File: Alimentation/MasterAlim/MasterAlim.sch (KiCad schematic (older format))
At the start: 42 parts, among them J1 Ext-Con, J10 Interf-Reg1, J11 AU Logic, J12 Interf-Reg2, J13 Interf-Reg3, J14 Interf-Reg4, J3 Bat. IN, J5 Direct Out, J6 Reg 1, J7 Reg 2, J8 Reg 3, J9 Reg 4, U1 74LS33, U3 ACS712xLCTR-20A, U6 PTN78020W_EUK-7, U7 ACS712xLCTR-20A

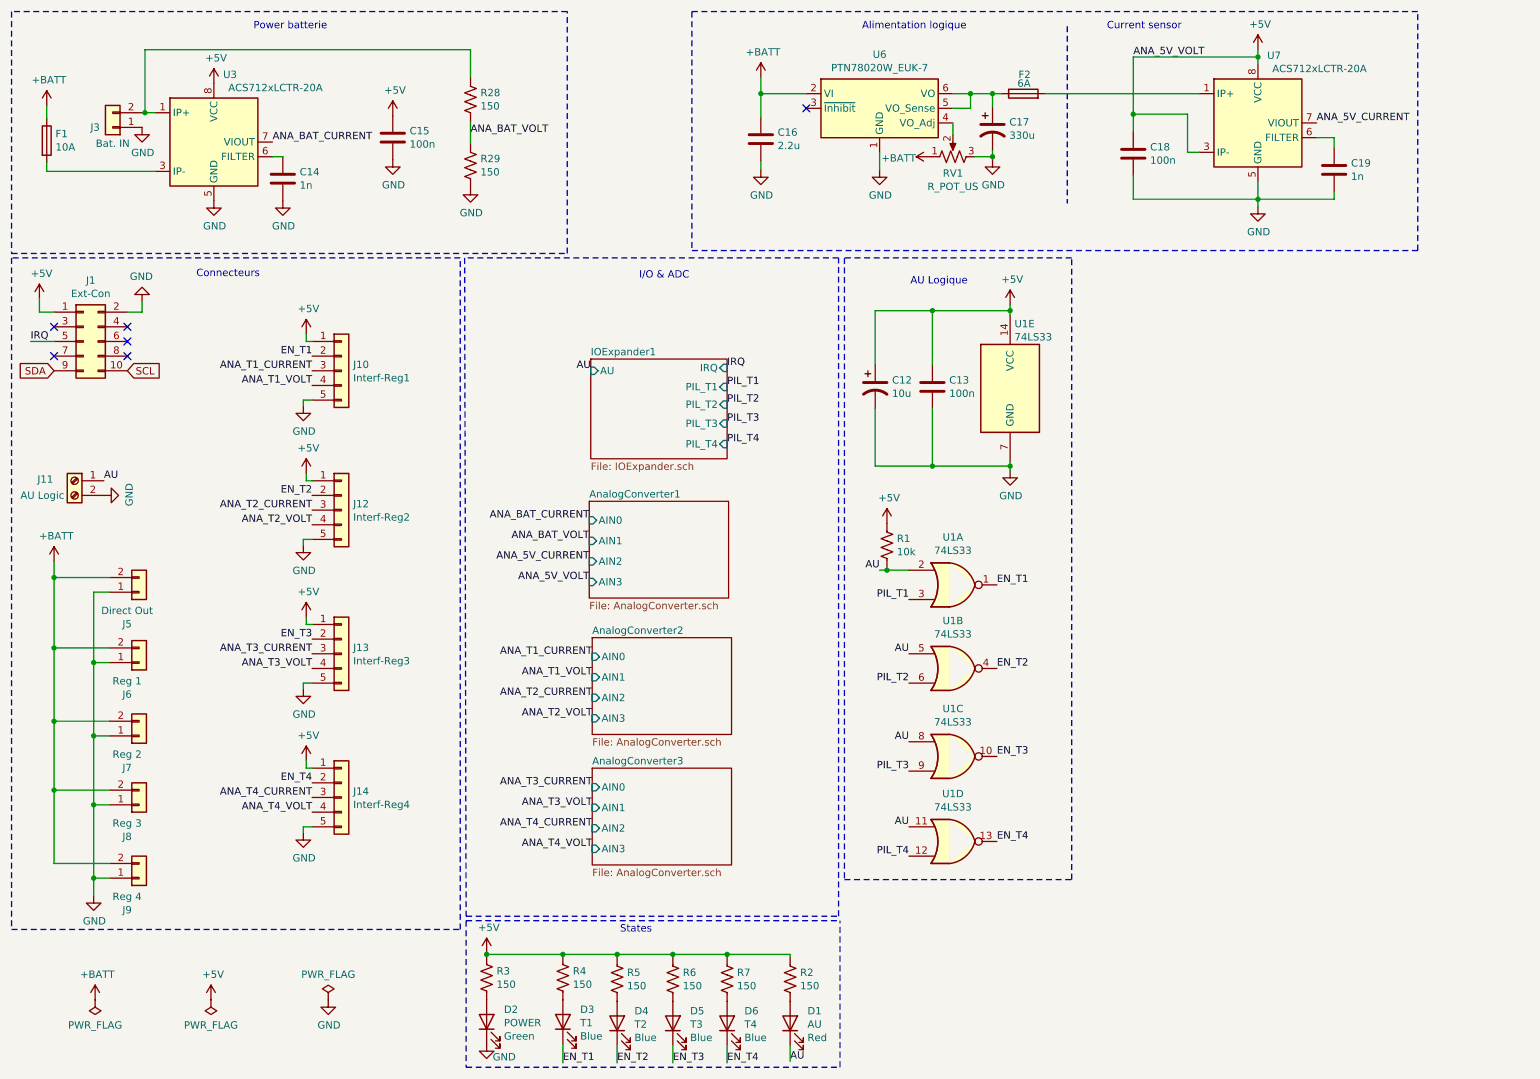
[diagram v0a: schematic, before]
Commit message: Dimensionnement et récupération des part LCSC
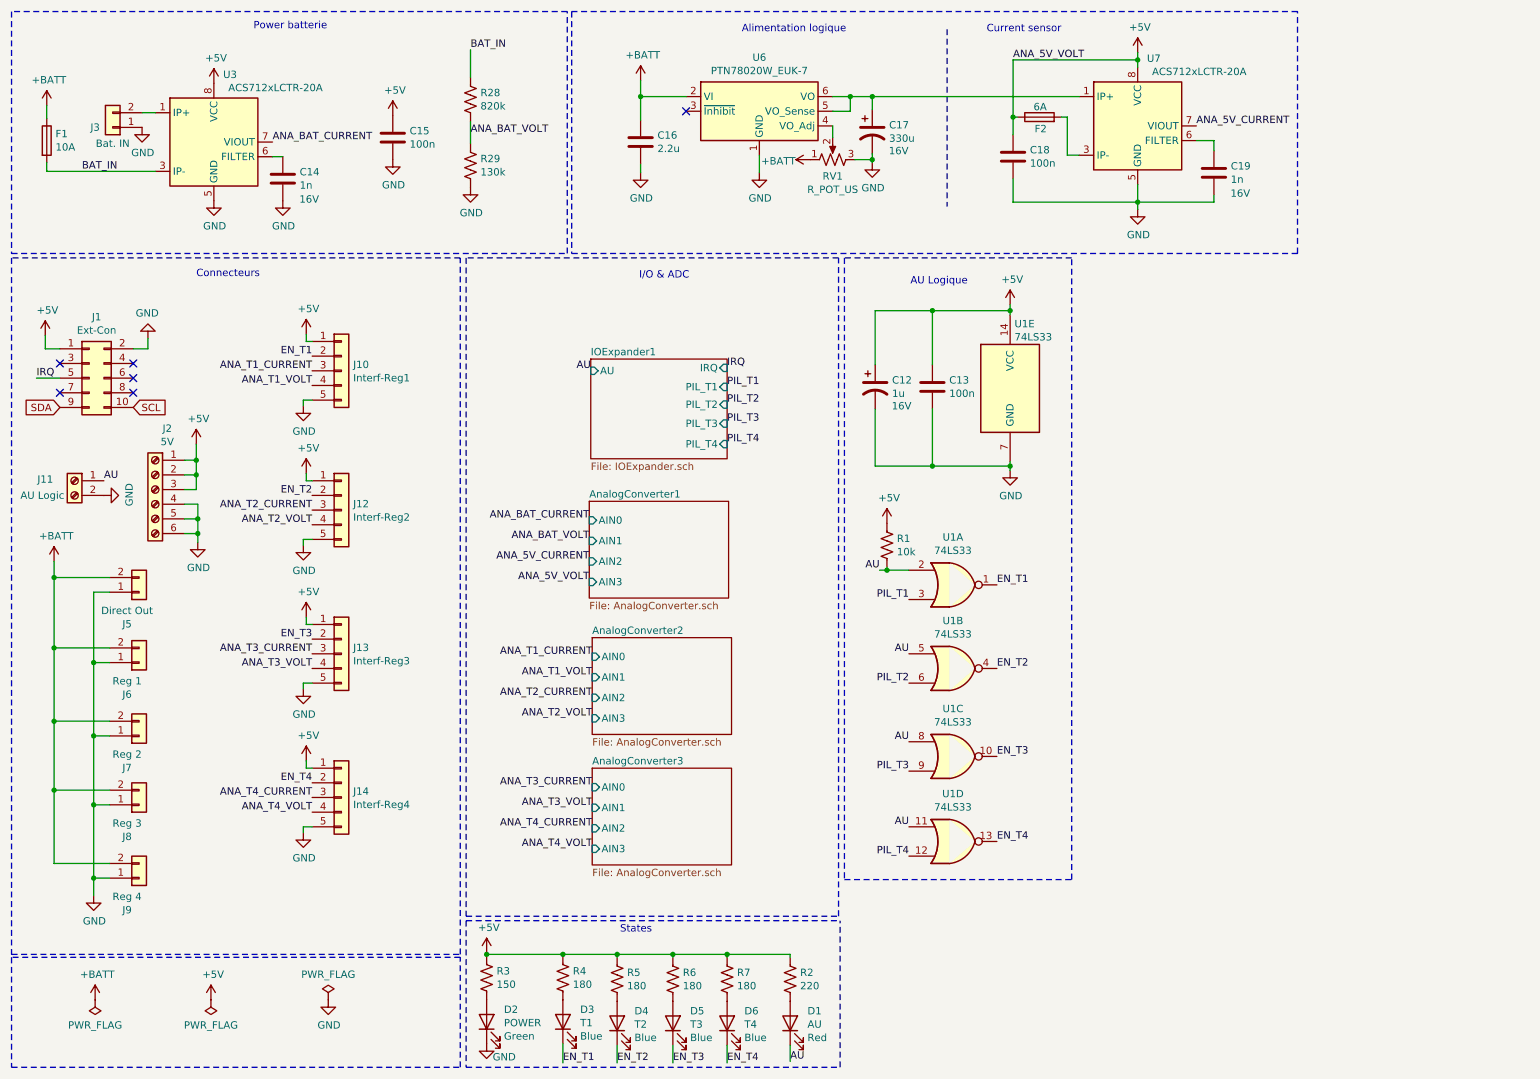
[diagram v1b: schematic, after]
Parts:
- added J2: 5V, TerminalBlock_Phoenix:TerminalBlock_Phoenix_MPT-0,5-6-2.54_1x06_P2.54mm_Horizontal, symbol Connector:Screw_Terminal_01x06
- C12: value 10u -> 1u; footprint (none) -> Capacitor_SMD:CP_Elec_4x5.3; LCSC Part (none) -> C249445; Tension (none) -> 16V
- C13, C15, C18: footprint Capacitor_SMD:C_0805_2012Metric -> Capacitor_SMD:C_0805_2012Metric_Pad1.18x1.45mm_HandSolder; LCSC Part (none) -> C28233
- C14: footprint (none) -> Capacitor_SMD:C_0603_1608Metric_Pad1.08x0.95mm_HandSolder; LCSC (none) -> C163169; Tension (none) -> 16V
- C16: footprint (none) -> Capacitor_SMD:C_0805_2012Metric_Pad1.18x1.45mm_HandSolder; LCSC Part (none) -> C508857; Tension (none) -> 50V
- C17: footprint (none) -> Capacitor_SMD:CP_Elec_10x10; LCSC Part (none) -> C249905; Tension (none) -> 16V
- C19: footprint (none) -> Capacitor_SMD:C_0603_1608Metric_Pad1.08x0.95mm_HandSolder; LCSC Part (none) -> C163169; Tension (none) -> 16V
- D1: LCSC Part (none) -> C72037
- D2: LCSC Part (none) -> C205442
- D3, D4, D5, D6: LCSC Part (none) -> C205441
- F1, F2, J1, J11, J3, J5, J6, J7, J8, J9, U1: JLCPCB BOM (none) -> 0
- J10, J12, J13, J14: footprint Connector_JST:JST_EH_S5B-EH_1x05_P2.50mm_Horizontal -> Connector_JST:JST_PH_B5B-PH-K_1x05_P2.00mm_Vertical; JLCPCB BOM (none) -> 0
- R1: footprint Resistor_SMD:R_0805_2012Metric -> Resistor_SMD:R_0805_2012Metric_Pad1.20x1.40mm_HandSolder; LCSC Part (none) -> C17414
- R2: value 150 -> 220; footprint Resistor_SMD:R_0805_2012Metric -> Resistor_SMD:R_0805_2012Metric_Pad1.20x1.40mm_HandSolder; LCSC Part (none) -> C417010
- R28: value 150 -> 820k; footprint Resistor_SMD:R_0805_2012Metric -> Resistor_SMD:R_0805_2012Metric_Pad1.20x1.40mm_HandSolder; LCSC Part (none) -> C334983
- R29: value 150 -> 130k; footprint Resistor_SMD:R_0805_2012Metric -> Resistor_SMD:R_0805_2012Metric_Pad1.20x1.40mm_HandSolder; LCSC Part (none) -> C25617
- R3: footprint Resistor_SMD:R_0805_2012Metric -> Resistor_SMD:R_0805_2012Metric_Pad1.20x1.40mm_HandSolder; LCSC Part (none) -> C17471
- R4, R5, R6, R7: value 150 -> 180; footprint Resistor_SMD:R_0805_2012Metric -> Resistor_SMD:R_0805_2012Metric_Pad1.20x1.40mm_HandSolder; LCSC Part (none) -> C168485
- RV1: footprint Potentiometer_THT:Potentiometer_Bourns_3299Y_Vertical -> Potentiometer_SMD:Potentiometer_Bourns_TC33X_Vertical; LCSC Part (none) -> C719177
- U6: footprint Module:Texas_EUK_R-PDSS-T7_THT -> ARIG:Texas_EUK_R-PDSS-T7_THT; JLCPCB BOM (none) -> 0
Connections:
- net +5V: now also F2.1, J2.1 (Pin_1), J2.2 (Pin_2), J2.3 (Pin_3); no longer U7.3 (IP-), U7.4 (IP-)
- net GND: now also J2.4 (Pin_4), J2.5 (Pin_5), J2.6 (Pin_6)
- net at J3.2 (Pin_2), U3.1 (IP+), U3.2 (IP+): no longer R28.1
- net at C17.1, U6.5 (VO_Sense), U6.6 (VO): now also U7.1 (IP+), U7.2 (IP+); no longer F2.1
- net BAT_IN: now reaches F1.2, U3.3 (IP-), U3.4 (IP-)
- net BAT_IN: now also R28.1
- new net: F2.2, U7.3 (IP-), U7.4 (IP-)
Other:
- moved on the sheet: C16, C17, C18, C19, F2, J1, RV1, U6, U7

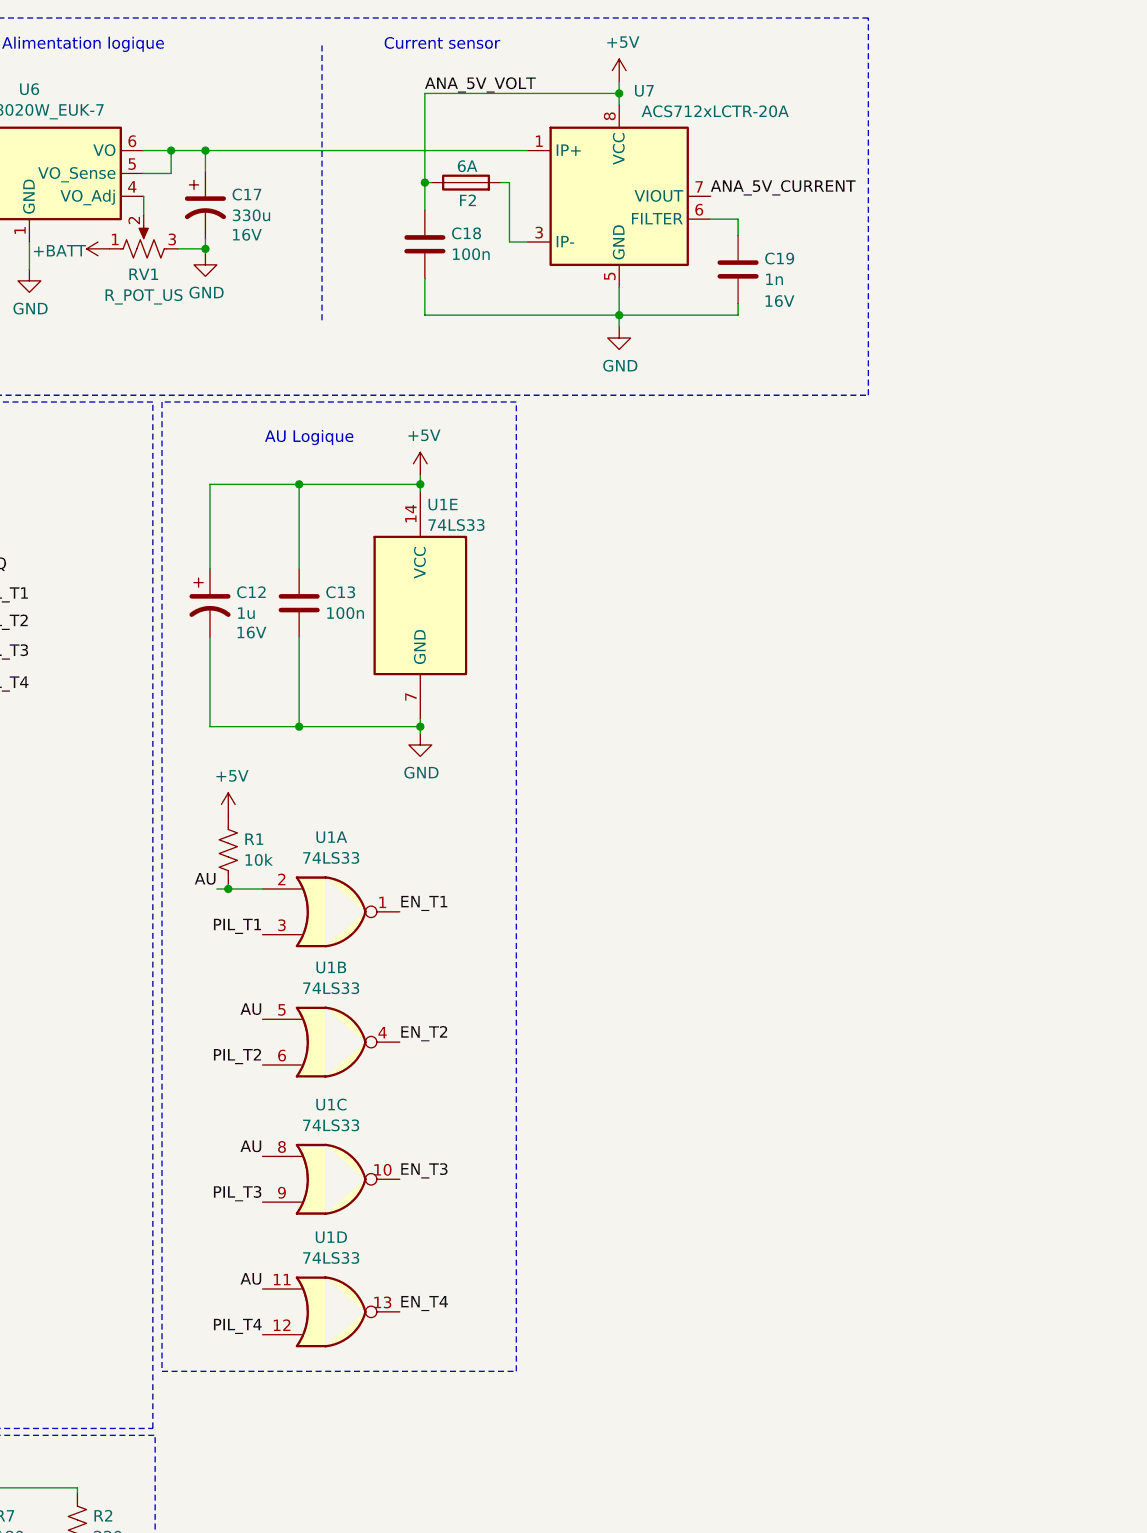
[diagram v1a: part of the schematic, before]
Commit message: Finalisation routage carte alim maitre
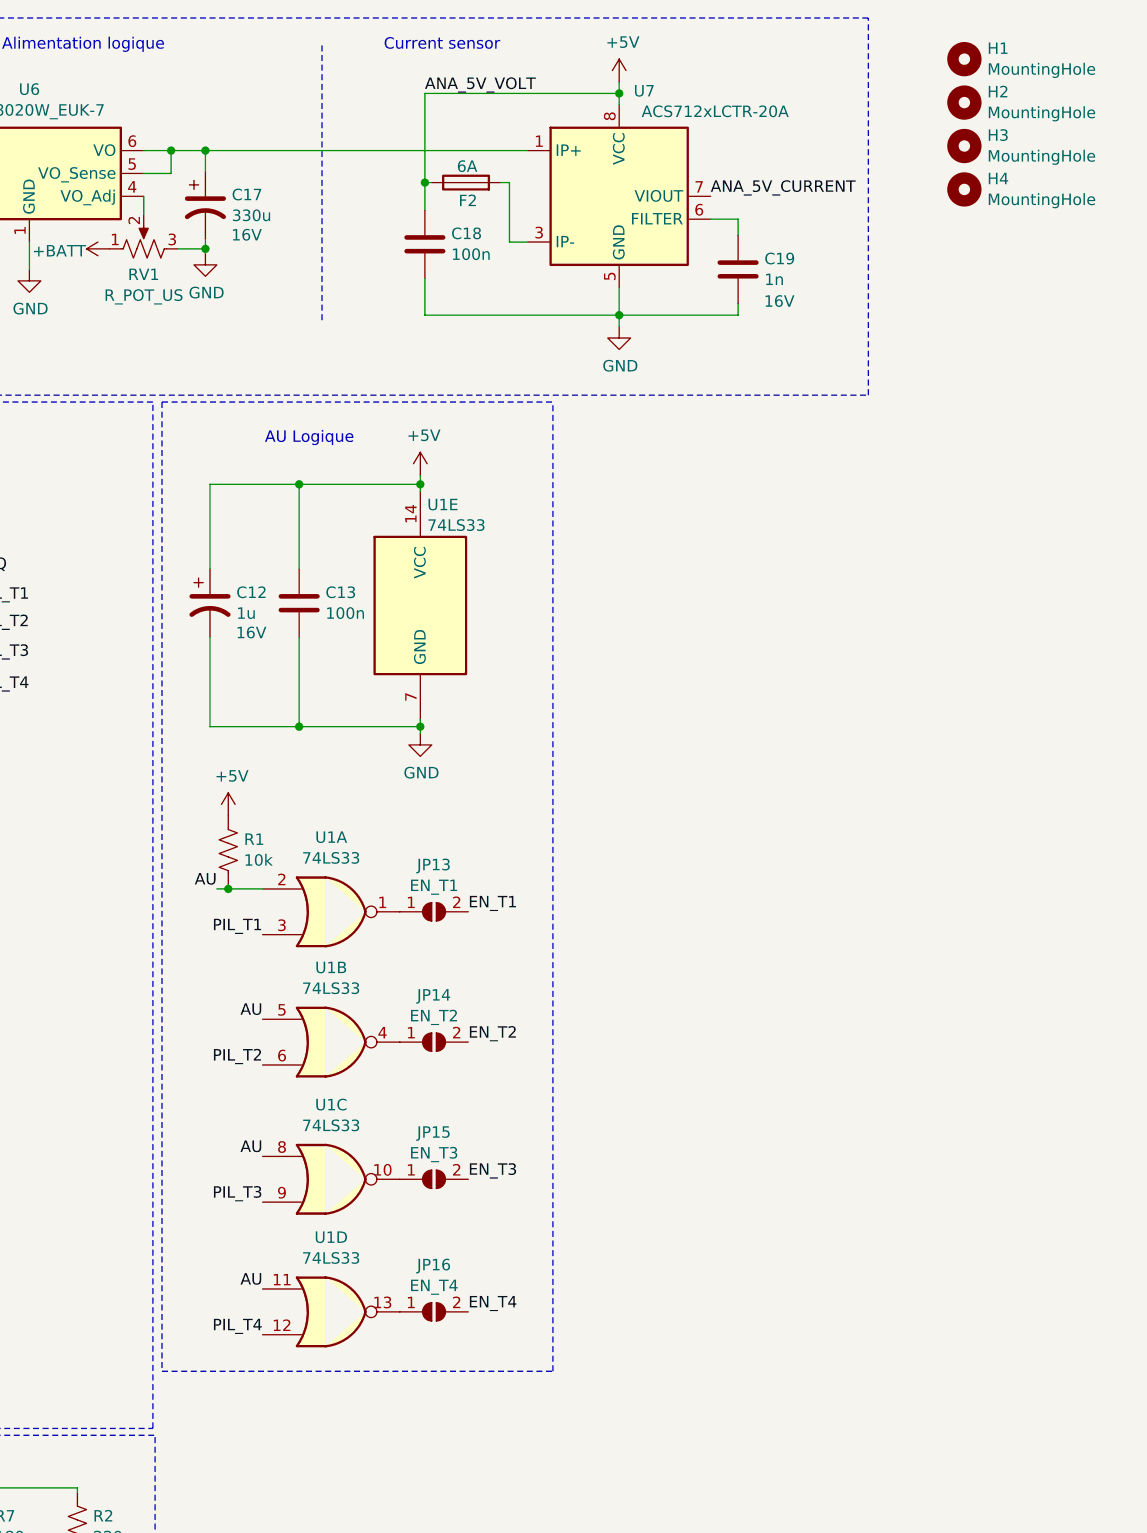
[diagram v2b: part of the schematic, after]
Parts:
- added H1, H2, H3, H4: MountingHole, MountingHole:MountingHole_3.2mm_M3, symbol Mechanical:MountingHole
- added JP13: EN_T1, Jumper:SolderJumper-2_P1.3mm_Open_RoundedPad1.0x1.5mm, symbol Jumper:SolderJumper_2_Open
- added JP14: EN_T2, Jumper:SolderJumper-2_P1.3mm_Open_RoundedPad1.0x1.5mm, symbol Jumper:SolderJumper_2_Open
- added JP15: EN_T3, Jumper:SolderJumper-2_P1.3mm_Open_RoundedPad1.0x1.5mm, symbol Jumper:SolderJumper_2_Open
- added JP16: EN_T4, Jumper:SolderJumper-2_P1.3mm_Open_RoundedPad1.0x1.5mm, symbol Jumper:SolderJumper_2_Open
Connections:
- net EN_T1: now also JP13.2 (B); no longer U1.1
- net EN_T2: now also JP14.2 (B); no longer U1.4
- net EN_T3: now also JP15.2 (B); no longer U1.10
- net EN_T4: now also JP16.2 (B); no longer U1.13
- new net: JP13.1 (A), U1.1
- new net: JP14.1 (A), U1.4
- new net: JP15.1 (A), U1.10
- new net: JP16.1 (A), U1.13
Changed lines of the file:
@@
 Text Label 7010 6320 2    50   ~ 0
 PIL_T4
-Text Label 7610 6220 0    50   ~ 0
+Text Label 7910 6220 0    50   ~ 0
 EN_T4
-Text Label 7610 5640 0    50   ~ 0
+Text Label 7910 5640 0    50   ~ 0
 EN_T3
-Text Label 7610 4470 0    50   ~ 0
+Text Label 7910 4470 0    50   ~ 0
 EN_T1
 Wire Notes Line
-	6570 6480 8120 6480
-Wire Notes Line
-	8120 6480 8120 2240
-Wire Notes Line
-	8120 2240 6570 2240
+	6570 6480 8280 6480
+Wire Notes Line
+	8280 6480 8280 2250
 Wire Notes Line
 	6570 2240 6570 6480
@@
 Wire Wire Line
 	5770 7010 5770 6990
-Text Label 7610 5040 0    50   ~ 0
+Text Label 7910 5040 0    50   ~ 0
 EN_T2
 $Comp
@@
 	2150 3820 2150 3720
 Connection ~ 2150 3720
+$Comp
+L Mechanical:MountingHole H1
+U 1 1 5FC2F35C
+P 10080 740
+F 0 "H1" H 10180 786 50  0000 L CNN
+F 1 "MountingHole" H 10180 695 50  0000 L CNN
+F 2 "MountingHole:MountingHole_3.2mm_M3" H 10080 740 50  0001 C CNN
+F 3 "~" H 10080 740 50  0001 C CNN
+	1    10080 740
+	1    0    0    -1
+$EndComp
+$Comp
+L Mechanical:MountingHole H2
+U 1 1 5FC311B6
+P 10080 930
+F 0 "H2" H 10180 976 50  0000 L CNN
+F 1 "MountingHole" H 10180 885 50  0000 L CNN
+F 2 "MountingHole:MountingHole_3.2mm_M3" H 10080 930 50  0001 C CNN
+F 3 "~" H 10080 930 50  0001 C CNN
+	1    10080 930
+	1    0    0    -1
+$EndComp
+$Comp
+L Mechanical:MountingHole H3
+U 1 1 5FC3153A
+P 10080 1120
+F 0 "H3" H 10180 1166 50  0000 L CNN
+F 1 "MountingHole" H 10180 1075 50  0000 L CNN
+F 2 "MountingHole:MountingHole_3.2mm_M3" H 10080 1120 50  0001 C CNN
+F 3 "~" H 10080 1120 50  0001 C CNN
+	1    10080 1120
+	1    0    0    -1
+$EndComp
+$Comp
+L Mechanical:MountingHole H4
+U 1 1 5FC3189D
+P 10080 1310
+F 0 "H4" H 10180 1356 50  0000 L CNN
+F 1 "MountingHole" H 10180 1265 50  0000 L CNN
+F 2 "MountingHole:MountingHole_3.2mm_M3" H 10080 1310 50  0001 C CNN
+F 3 "~" H 10080 1310 50  0001 C CNN
+	1    10080 1310
+	1    0    0    -1
+$EndComp
+$Comp
+L Jumper:SolderJumper_2_Open JP13
+U 1 1 5FC8DEE2
+P 7760 4470
+F 0 "JP13" H 7760 4675 50  0000 C CNN
+F 1 "EN_T1" H 7760 4584 50  0000 C CNN
+F 2 "Jumper:SolderJumper-2_P1.3mm_Open_RoundedPad1.0x1.5mm" H 7760 4470 50  0001 C CNN
+F 3 "~" H 7760 4470 50  0001 C CNN
+	1    7760 4470
+	1    0    0    -1
+$EndComp
+$Comp
+L Jumper:SolderJumper_2_Open JP14
+U 1 1 5FCA7ABF
+P 7760 5040
+F 0 "JP14" H 7760 5245 50  0000 C CNN
+F 1 "EN_T2" H 7760 5154 50  0000 C CNN
+F 2 "Jumper:SolderJumper-2_P1.3mm_Open_RoundedPad1.0x1.5mm" H 7760 5040 50  0001 C CNN
+F 3 "~" H 7760 5040 50  0001 C CNN
+	1    7760 5040
+	1    0    0    -1
+$EndComp
+$Comp
+L Jumper:SolderJumper_2_Open JP15
+U 1 1 5FCA8A3F
+P 7760 5640
+F 0 "JP15" H 7760 5845 50  0000 C CNN
+F 1 "EN_T3" H 7760 5754 50  0000 C CNN
+F 2 "Jumper:SolderJumper-2_P1.3mm_Open_RoundedPad1.0x1.5mm" H 7760 5640 50  0001 C CNN
+F 3 "~" H 7760 5640 50  0001 C CNN
+	1    7760 5640
+	1    0    0    -1
+$EndComp
+$Comp
+L Jumper:SolderJumper_2_Open JP16
+U 1 1 5FCA9630
+P 7760 6220
+F 0 "JP16" H 7760 6425 50  0000 C CNN
+F 1 "EN_T4" H 7760 6334 50  0000 C CNN
+F 2 "Jumper:SolderJumper-2_P1.3mm_Open_RoundedPad1.0x1.5mm" H 7760 6220 50  0001 C CNN
+F 3 "~" H 7760 6220 50  0001 C CNN
+	1    7760 6220
+	1    0    0    -1
+$EndComp
+Wire Notes Line
+	6570 2240 8280 2240
 $EndSCHEMATC
